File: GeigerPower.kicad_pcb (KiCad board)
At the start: 2 copper layers, 42 parts, among them J1 ConnBat, J2 ConnPulse, Q1 BC817, Q2 MMBTA42, U1 40106

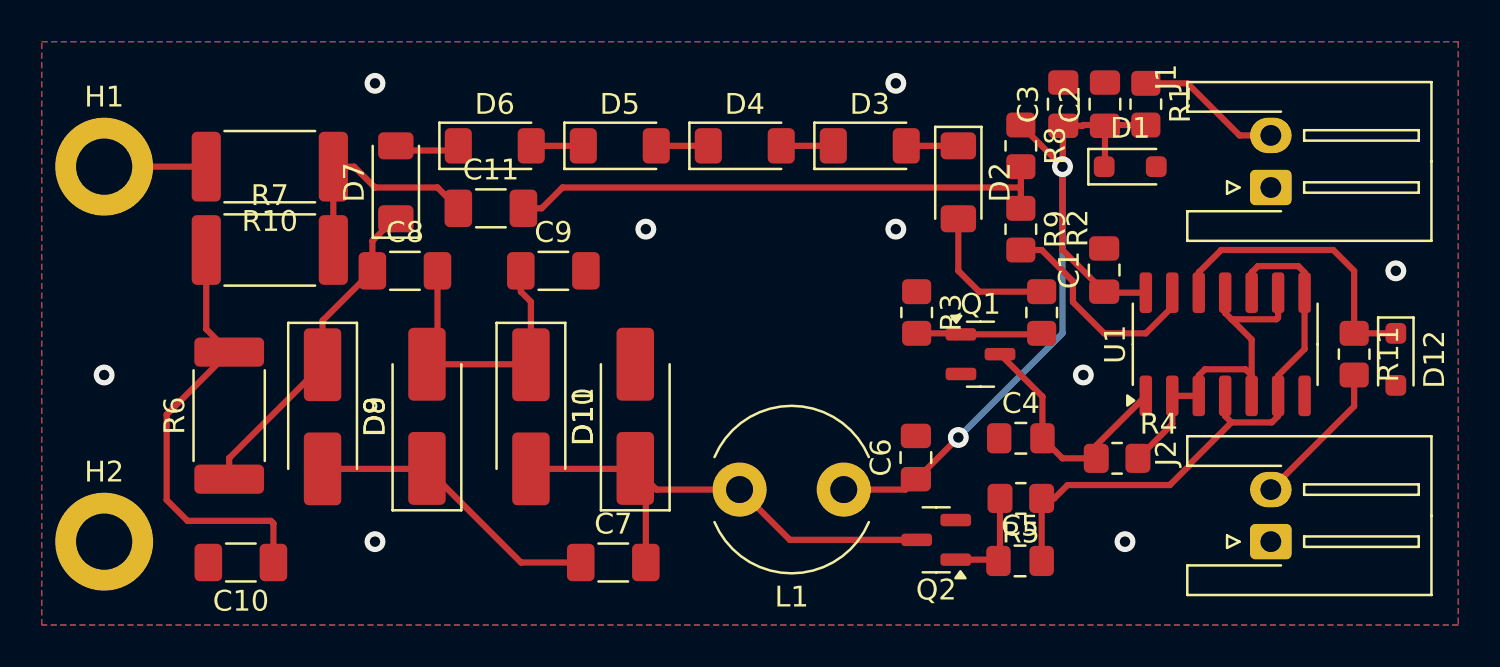
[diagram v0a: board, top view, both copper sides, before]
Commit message: Update GeigerPower.kicad_pcb
Added conotur. Compactified a bit the layout. Placed silkscreen data.
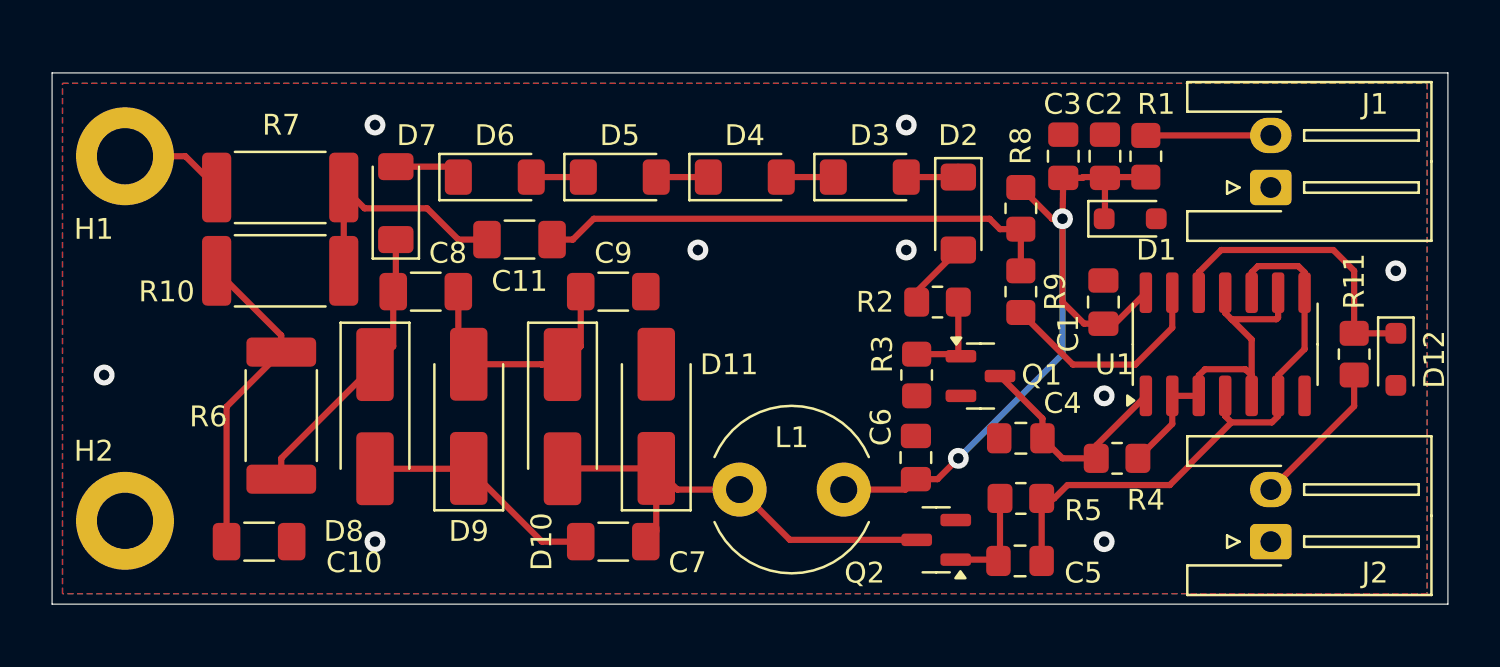
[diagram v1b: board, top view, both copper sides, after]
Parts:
- moved R2 5.02 mm to (72.0, 55.5), turned to 0 degrees
- moved C9 3.04 mm to (56.4, 55.0)
- moved R3 3.00 mm to (71.0, 59.0), turned to 90 degrees
- moved R8 3.00 mm to (76.0, 51.0)
- moved R9 3.00 mm to (76.0, 55.0)
- moved D8 2.52 mm to (45.0, 61.0)
- moved C2 2.50 mm to (80.0, 48.5)
- moved C3 2.50 mm to (78.0, 48.5)
- moved D1 2.50 mm to (81.2, 51.5)
- moved R1 2.50 mm to (82.0, 48.5)
- moved R6 2.50 mm to (40.5, 61.0)
- moved C11 2.03 mm to (51.9, 52.5)
- moved D9 2.01 mm to (49.5, 61.0)
- moved C1 1.54 mm to (80.0, 55.5)
- moved D10 1.52 mm to (54.0, 61.0)
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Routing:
- net Net-(C10-Pad1): track 21.2 -> 15.4 mm
- net Net-(D2-A): track 7.41 -> 3.33 mm
- net Net-(D8-A): track 14.3 -> 11.3 mm
- net Net-(D10-A): track 24.7 -> 22.1 mm
- net Net-(D10-K): track 14.4 -> 12.1 mm
- net VCC: track 41.3 -> 39.3 mm
- net Net-(D7-K): track 15.5 -> 13.8 mm
- net Net-(Q1-B): track 6.04 -> 4.82 mm
- net Net-(C11-Pad2): track 26.3 -> 25.1 mm
- net Net-(C11-Pad1): track 10.8 -> 11.9 mm
- net Net-(Q1-C): track 11.8 -> 10.8 mm
- net +BATT: track 7.04 -> 6.00 mm
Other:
- board outline added: 67 x 25.5 mm

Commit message: Adjustments, HV-rules
Added high coltage rules. Small silkscreen fixes applied. Another contour edit performed.
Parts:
- moved J1 0.50 mm to (88.0, 50.5)
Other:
- board size 67 x 25.5 mm -> 67 x 25 mm
- board text added: "+400V"
- board text added: "0V"
